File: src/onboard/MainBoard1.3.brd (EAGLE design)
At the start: 134.6 x 80.5 mm, 87 parts, among them IC1 MIC29310-5.0BT, IC3 A5975D, U1 ADAFRUIT_BMP280_BAROMETER

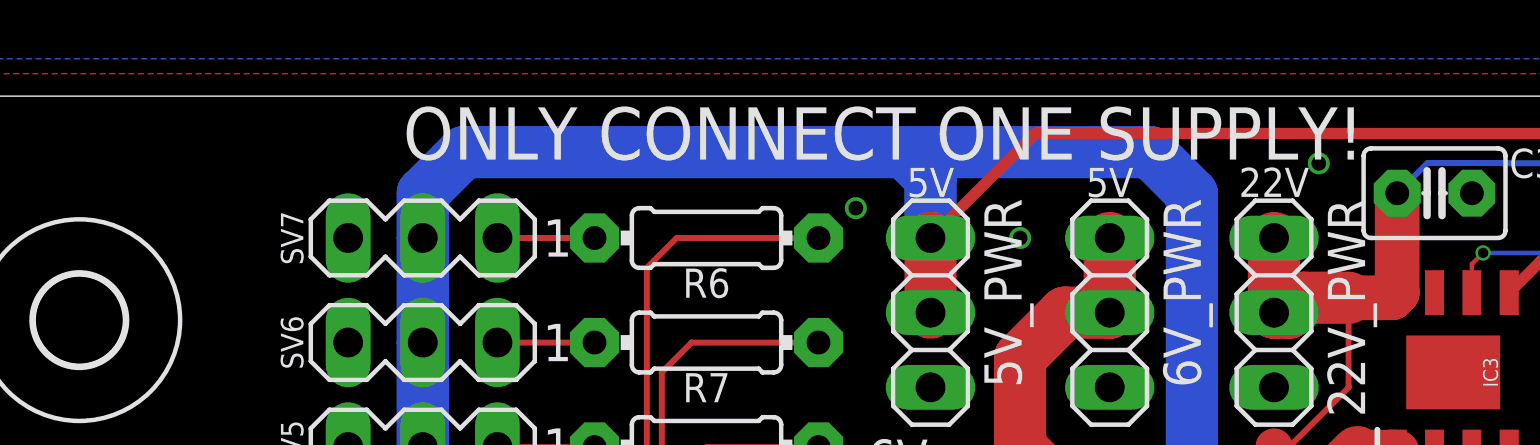
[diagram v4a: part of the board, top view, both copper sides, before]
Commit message: Moved power supply silkscreen for visibility
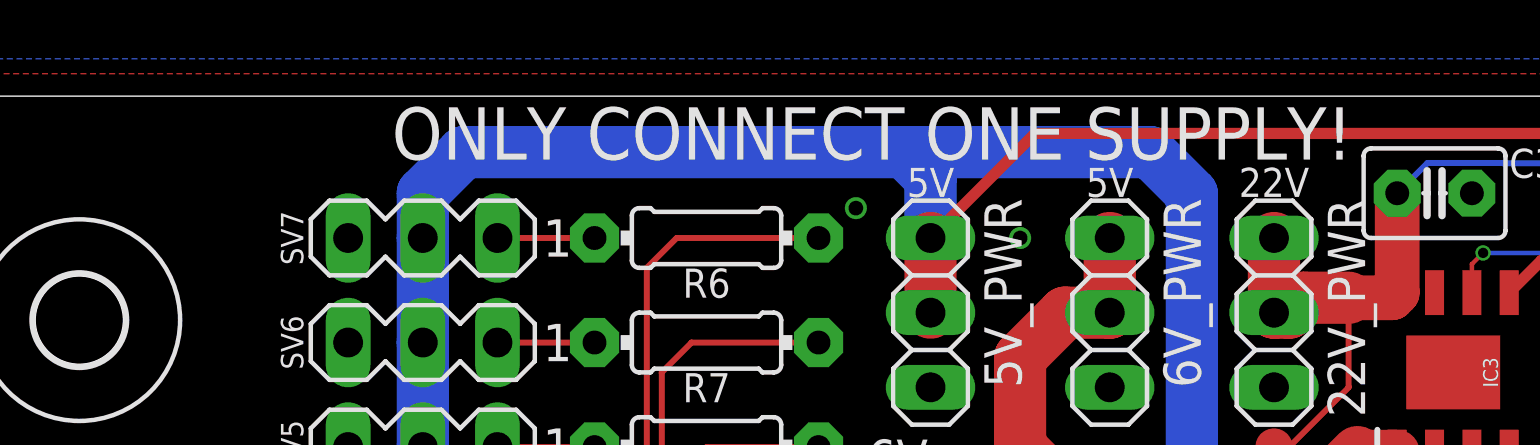
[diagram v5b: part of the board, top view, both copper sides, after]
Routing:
- net GND: vias 142 -> 141
